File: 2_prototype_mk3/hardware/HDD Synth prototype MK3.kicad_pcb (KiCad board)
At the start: 2 copper layers, 157.5 x 97.8 mm, 47 parts, among them J1 Micro_SD_Card, J3 Bus_ISA_8bit, SW1 SW_Push, U1 Optocoupler_DC_PhotoNPN_AKEC, U5 MAX98357A, U6 74LS573, U7 74LS573, U8 ATF22V10C-10PU

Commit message: MKIII design refinements
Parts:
- removed the   at (140.8, 59.6) (x2)
- added G***: LOGO, HDDSyncMKIII:MKIII logo - 20mm, F.Cu at (85.0, 116.8)
- added G***: LOGO, HDDSyncMKIII:MKIII logo - 30mm, F.Cu at (172.6, 93.9)
- J3: footprint Connector_PCBEdge:BUS_AT -> HDDSyncMKIII:BUS_AT_8bit
- moved H3 52.2 mm to (206.9, 116.8)
- moved C1 51.1 mm to (173.1, 60.6)
- moved FB2 51.1 mm to (173.0, 56.8)
- moved C2 51.1 mm to (173.1, 49.2)
- moved FB1 51.1 mm to (173.0, 52.8)
- moved H6 50.8 mm to (165.0, 53.3)
- moved C6 49.4 mm to (177.7, 47.9), turned to -90 degrees
- moved U5 49.1 mm to (180.1, 55.0)
- moved C5 48.2 mm to (181.5, 47.9), turned to -90 degrees
- moved G*** 37.6 mm to (175.1, 104.1)
- moved   37.5 mm to (133.5, 59.5)
- moved U8 27.4 mm to (159.9, 125.7), turned to 90 degrees
- moved C12 26.5 mm to (157.4, 113.8), turned to 90 degrees
- moved D5 22.3 mm to (162.4, 111.8), turned to -90 degrees
- moved H1 17.8 mm to (179.0, 68.4)
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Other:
- board size 157.5 x 97.8 mm -> 119.4 x 97.8 mm
- board text added: "Make sure the edge cuts for the slot are ok"

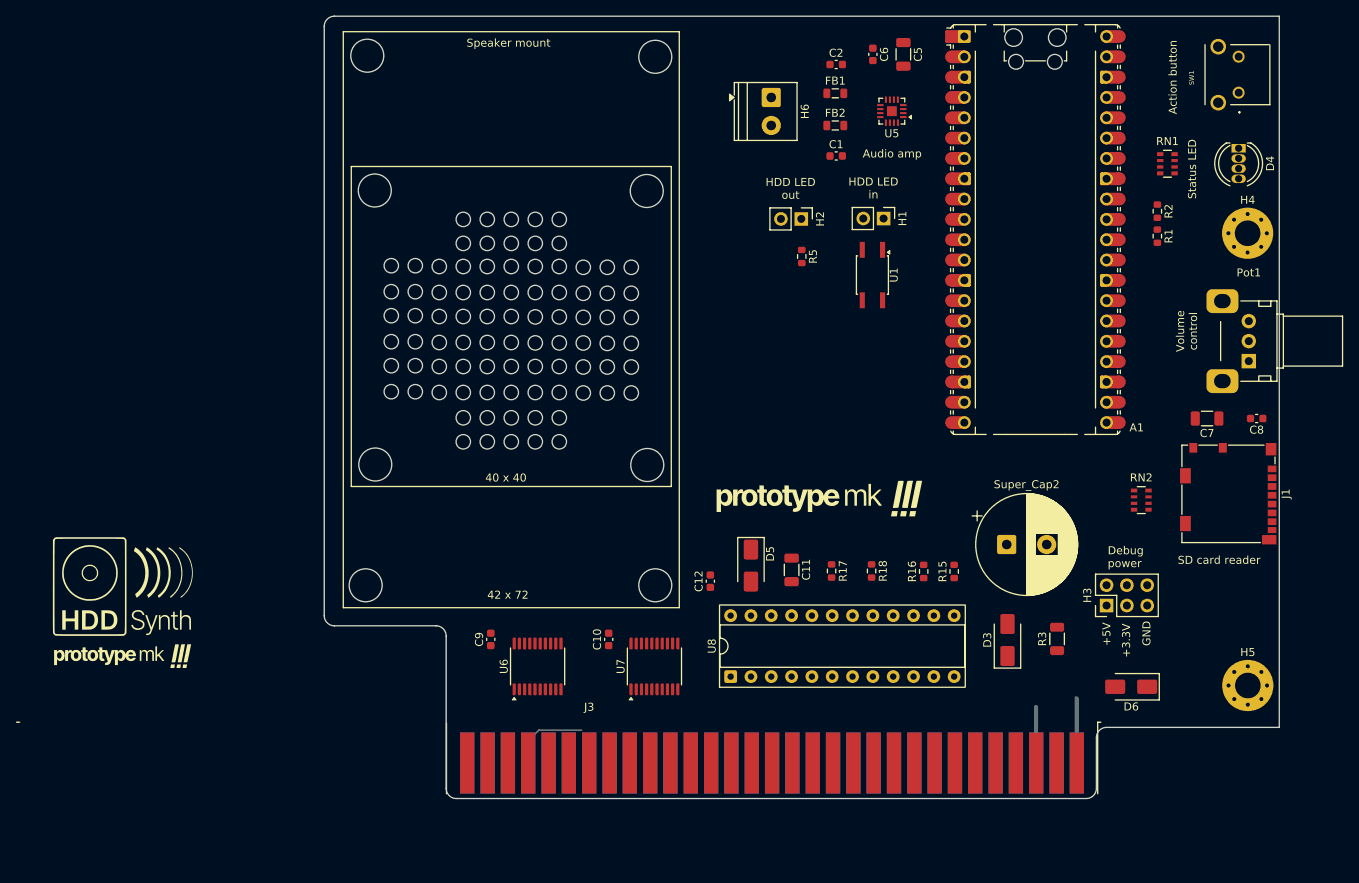
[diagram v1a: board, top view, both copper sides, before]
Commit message: Add net classes for power
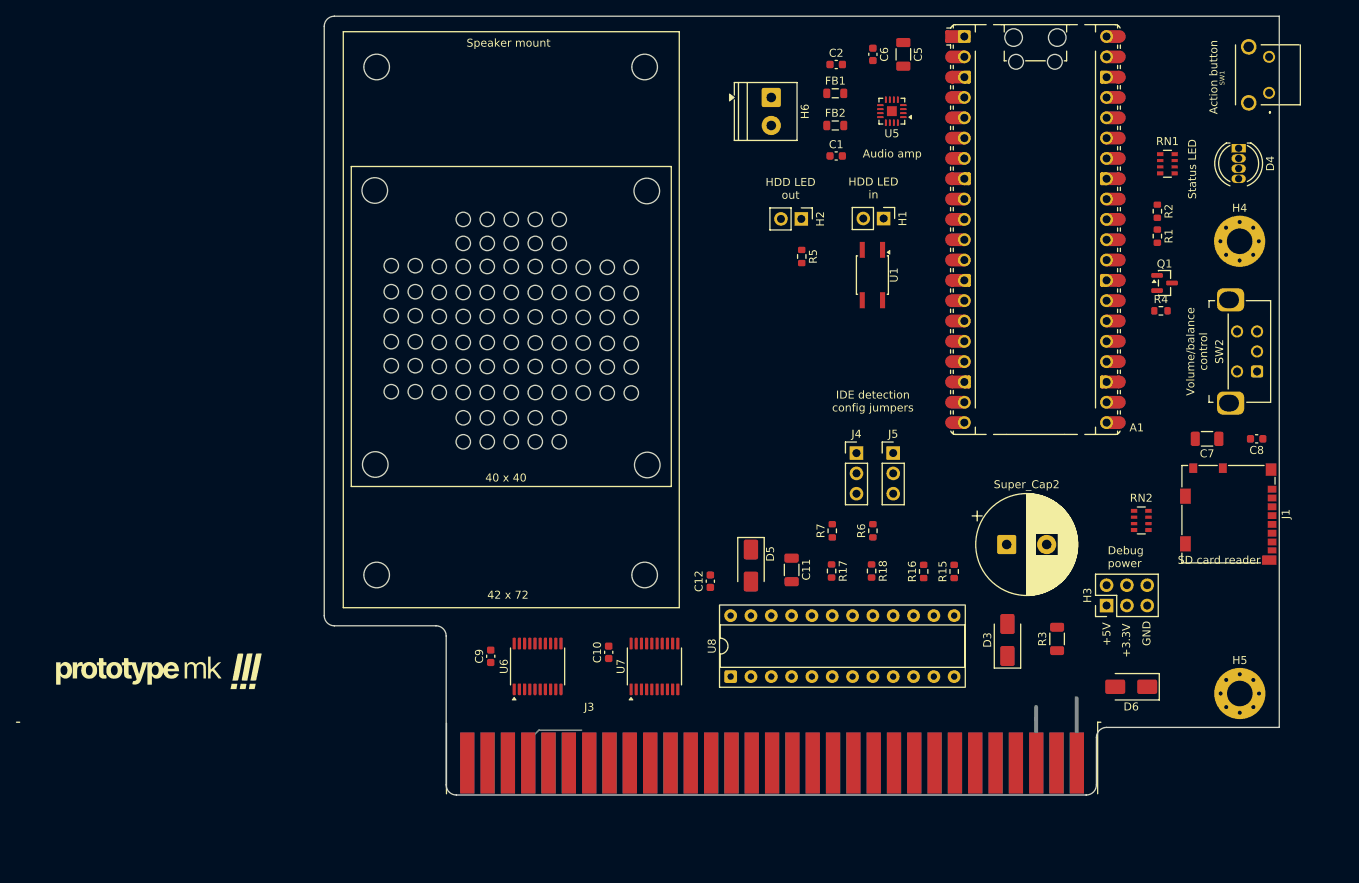
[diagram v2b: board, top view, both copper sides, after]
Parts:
- removed the G*** at (85.0, 116.8)
- removed Pot1: R_Potentiometer, Potentiometer_THT:Potentiometer_Alps_RK09K_Single_Horizontal
- added H10: MountingHole, MountingHole:MountingHole_3.2mm_M3, F.Cu at (149.5, 99.2)
- added H11: MountingHole, MountingHole:MountingHole_3.2mm_M3, F.Cu at (115.7, 49.5)
- added H12: MountingHole, MountingHole:MountingHole_3.2mm_M3, F.Cu at (149.2, 49.5)
- added H13: MountingHole, MountingHole:MountingHole_3.2mm_M3, F.Cu at (115.7, 113.0)
- added H14: MountingHole, MountingHole:MountingHole_3.2mm_M3, F.Cu at (149.2, 113.0)
- added H7: MountingHole, MountingHole:MountingHole_3.2mm_M3, F.Cu at (115.4, 64.9)
- added H8: MountingHole, MountingHole:MountingHole_3.2mm_M3, F.Cu at (149.4, 65.0)
- added H9: MountingHole, MountingHole:MountingHole_3.2mm_M3, F.Cu at (115.5, 99.2)
- added J4: Conn_01x03, Connector_PinHeader_2.54mm:PinHeader_1x03_P2.54mm_Vertical, F.Cu at (175.6, 97.8)
- added J5: Conn_01x03, Connector_PinHeader_2.54mm:PinHeader_1x03_P2.54mm_Vertical, F.Cu at (180.2, 97.8)
- added Q1: 2N3904, Package_TO_SOT_SMD:SOT-23, F.Cu at (214.1, 76.5)
- added R4: 10K, Resistor_SMD:R_0603_1608Metric, F.Cu at (213.7, 80.0)
- added R6: 330R, Resistor_SMD:R_0603_1608Metric, F.Cu at (177.7, 107.5)
- added R7: 3.3K, Resistor_SMD:R_0603_1608Metric, F.Cu at (172.6, 107.5)
- added SW2: RotaryEncoder_Switch, Rotary_Encoder:RotaryEncoder_Bourns_Horizontal_PEC12R-2x17F-Sxxxx, F.Cu at (225.7, 87.5)
- C11: value 10uF -> 2.2uF
- R18: value 330R -> 2.2K
- moved G*** 85.3 mm to (90.0, 115.5)
- moved G*** 36.1 mm to (140.8, 115.5)
- moved SW1 3.81 mm to (227.2, 52.7)
- moved J1 2.54 mm to (222.1, 105.4)
- moved RN2 2.54 mm to (211.2, 106.2)
- moved C7 2.54 mm to (219.5, 96.0)
- moved C8 2.54 mm to (225.7, 96.0)
- moved C9 2.11 mm to (129.9, 123.2)
- moved C10 1.61 mm to (144.7, 122.7)
- moved H4 1.41 mm to (223.5, 71.3)
- moved H5 1.41 mm to (223.5, 127.8)
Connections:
- A1 pad 26: unconnected-(A1-GPIO20-Pad26) -> /ENC_A
- A1 pad 27: unconnected-(A1-GPIO21-Pad27)_1 -> /ENC_B
- A1 pad 29: unconnected-(A1-GPIO22-Pad29)_1 -> /ENC_SWITCH
- A1 pad 30: unconnected-(A1-RUN-Pad30)_1 -> Net-(A1-RUN)
- A1 pad 32: /VOL_POT -> unconnected-(A1-GPIO27_ADC1-Pad32)
- D5 pad 2: /ISA IDE activity detection/IDE_ACTIVITY_RAW -> Net-(D5-A)
- J1 pad 2: /SD card reader/SD_CS -> /SD_CS
- J3 pad 2: unconnected-(J3-RESET-Pad2) -> /ISA IDE activity detection/RESET
- RN2 pad 1: /SD card reader/SD_CS -> /SD_CS
- U8 pad 21: unconnected-(U8-IO7-Pad21) -> Net-(J4-Pin_2)
- U8 pad 22: /ISA IDE activity detection/IDE_ACTIVITY_RAW -> Net-(J5-Pin_2)
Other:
- board size 119.4 x 97.8 mm -> 119.4 x 97.4 mm
- board text added: "IDE detection config jumpers"
- board text added: "Special thanks to: - Cecilia MacLoughlin - Ian (polpo) Scott - Ian (PSYCHROME) Ball - Mark Angus - Neil Thomas (Retro Collective) - vswitchzero - Wouter Groeneveld - VOGONS and SWAG"
- board text added: "Volume/balance control"
- board text added: "www.strifestreams.com/hddsynth"
- board text removed: "Volume control"

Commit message: MKIII PCB components connected and passing DRC
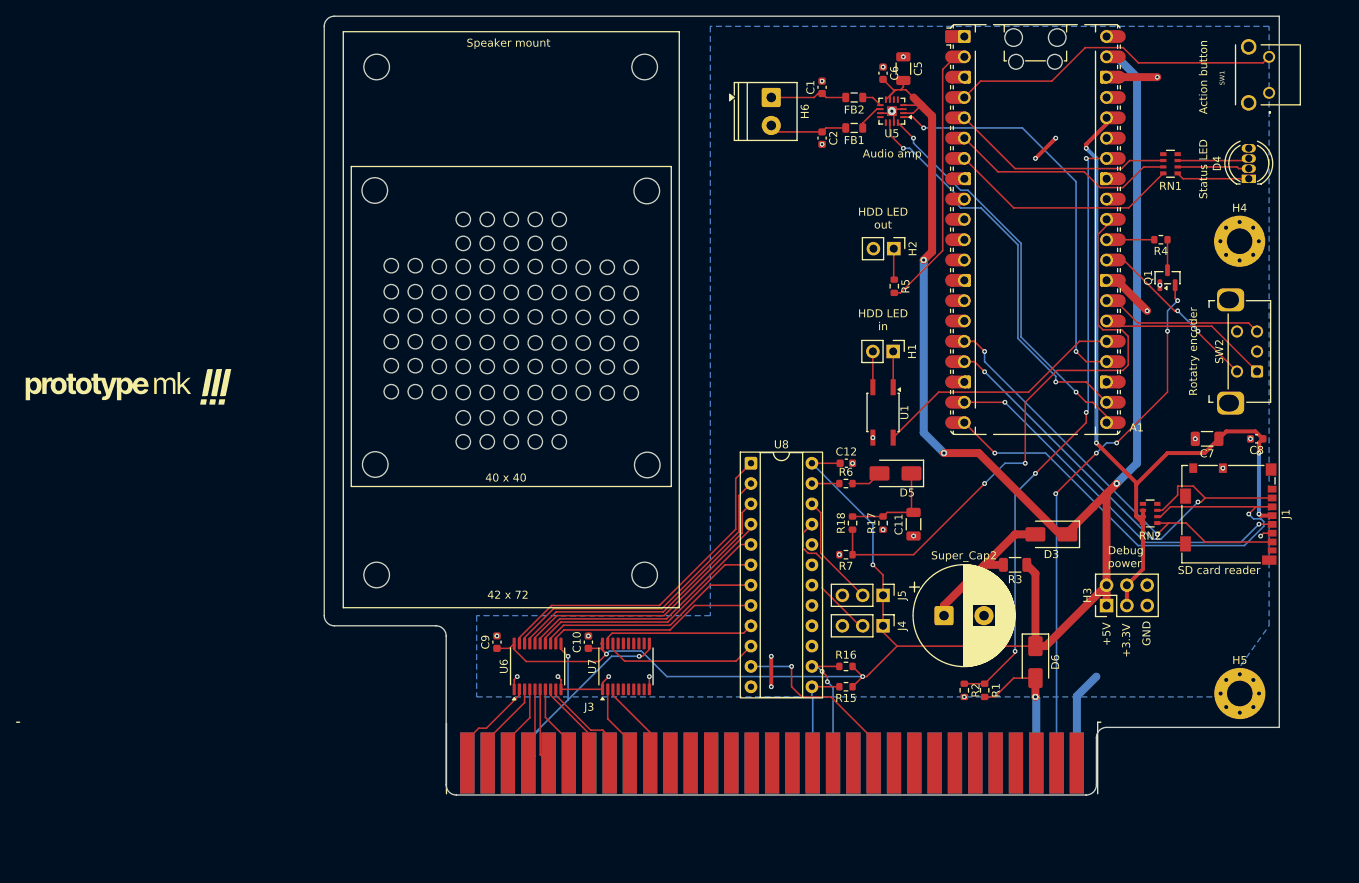
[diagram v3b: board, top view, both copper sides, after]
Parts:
- moved R2 64.6 mm to (189.1, 127.4)
- moved R1 60.7 mm to (191.7, 127.4)
- moved G*** 35.8 mm to (86.2, 80.0)
- moved U8 26.8 mm to (162.4, 99.0), turned to 0 degrees
- moved C12 22.5 mm to (174.4, 99.0), turned to 0 degrees
- moved J4 21.8 mm to (178.9, 119.3), turned to -90 degrees
- moved D5 21.4 mm to (180.5, 100.3), turned to 180 degrees
- moved R15 19.8 mm to (174.3, 127.0), turned to 180 degrees
- moved J5 17.8 mm to (178.9, 115.5), turned to -90 degrees
- moved U1 17.2 mm to (178.9, 92.7)
- moved H1 16.7 mm to (180.2, 85.0)
- moved C11 16.3 mm to (182.8, 106.6), turned to 90 degrees
- moved R16 15.3 mm to (174.3, 124.4), turned to 0 degrees
- moved D3 14.3 mm to (200.0, 107.9), turned to 180 degrees
- moved D6 12.4 mm to (198.0, 123.9), turned to -90 degrees
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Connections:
- A1 pad 39: /Power management/VSYS_5V_INPUT -> POWER_5V_SUP
- C1 pad 1: Net-(H6-Pin_2) -> Net-(H6-Pin_1)
- C10 pad 1: +5V -> POWER_5V_SUP
- C12 pad 1: +5V -> POWER_5V_SUP
- C2 pad 1: Net-(H6-Pin_1) -> Net-(H6-Pin_2)
- C5 pad 2: +5V -> POWER_5V_SUP
- C6 pad 2: +5V -> POWER_5V_SUP
- C9 pad 1: +5V -> POWER_5V_SUP
- D3 pad 1: /Power management/VSYS_5V_INPUT -> POWER_5V_SUP
- D6 pad 1: /Power management/VSYS_5V_INPUT -> POWER_5V_SUP
- FB1 pad 2: Net-(H6-Pin_1) -> Net-(H6-Pin_2)
- FB2 pad 2: Net-(H6-Pin_2) -> Net-(H6-Pin_1)
- H3 pad 1: /Power management/VSYS_5V_INPUT -> POWER_5V_SUP
- H3 pad 2: /Power management/VSYS_5V_INPUT -> POWER_5V_SUP
- J4 pad 1: +5V -> POWER_5V_SUP
- J5 pad 1: +5V -> POWER_5V_SUP
- R15 pad 1: +5V -> POWER_5V_SUP
- R16 pad 2: +5V -> POWER_5V_SUP
- R3 pad 1: /Power management/VSYS_5V_INPUT -> POWER_5V_SUP
- RN2 pad 1: /SD_CS -> /SD_SO
- RN2 pad 3: /SD_SO -> /SD_CS
- U5 pad 2: +5V -> POWER_5V_SUP
- U5 pad 4: +5V -> POWER_5V_SUP
- U5 pad 7: +5V -> POWER_5V_SUP
- U5 pad 8: +5V -> POWER_5V_SUP
- U6 pad 20: +5V -> POWER_5V_SUP
- U7 pad 20: +5V -> POWER_5V_SUP
- U8 pad 24: +5V -> POWER_5V_SUP
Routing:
- net POWER_5V_SUP: track 0.00 -> 295.1 mm, vias 0 -> 6
- net +3.3V: track 0.00 -> 98.0 mm, vias 0 -> 4
- net /ISA_VCC_DETECT: track 0.00 -> 76.2 mm, vias 0 -> 4
- net /IDE_ACTIVITY: track 0.00 -> 74.5 mm, vias 0 -> 2
- net /ISA IDE activity detection/RESET: track 0.00 -> 67.0 mm, vias 0 -> 5
- net /SD_SI: track 0.00 -> 63.8 mm, vias 0 -> 2
- net /SD_CS: track 0.00 -> 58.3 mm, vias 0 -> 2
- net /SD_SO: track 0.00 -> 52.2 mm, vias 0 -> 2
- net /AMP_DIN: track 0.00 -> 50.5 mm, vias 0 -> 2
- net /AMP_LRC: track 0.00 -> 50.4 mm, vias 0 -> 2
- net /AMP_BCLK: track 0.00 -> 49.6 mm, vias 0 -> 2
- net /SD_CLK: track 0.00 -> 46.7 mm, vias 0 -> 2
- net /ISA IDE activity detection/ISA_AL0: track 0.00 -> 42.4 mm
- net GND: track 8.32 -> 50.6 mm, vias 0 -> 28
- net /ACTION_BUTTON: track 0.00 -> 41.8 mm
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- added copper zone on B.Cu, net GND
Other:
- board text added: "Rotatry encoder"
- board text removed: "IDE detection config jumpers"
- board text removed: "Volume/balance control"

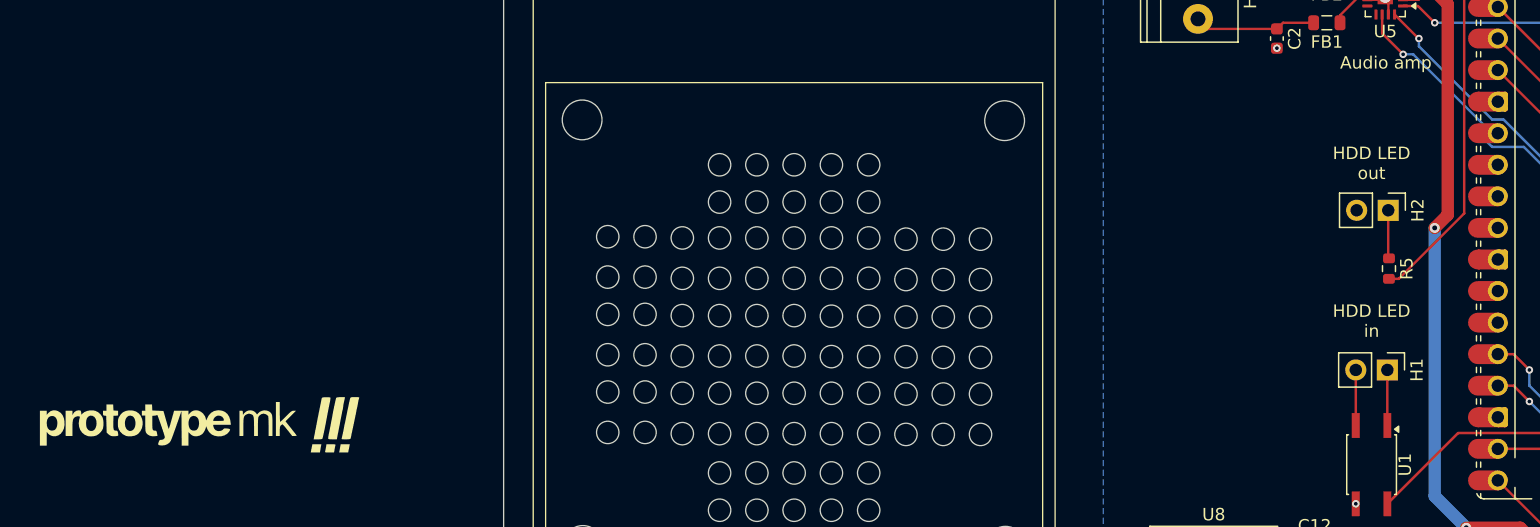
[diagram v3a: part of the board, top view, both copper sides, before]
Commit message: Finalise silk screen and tidy up files
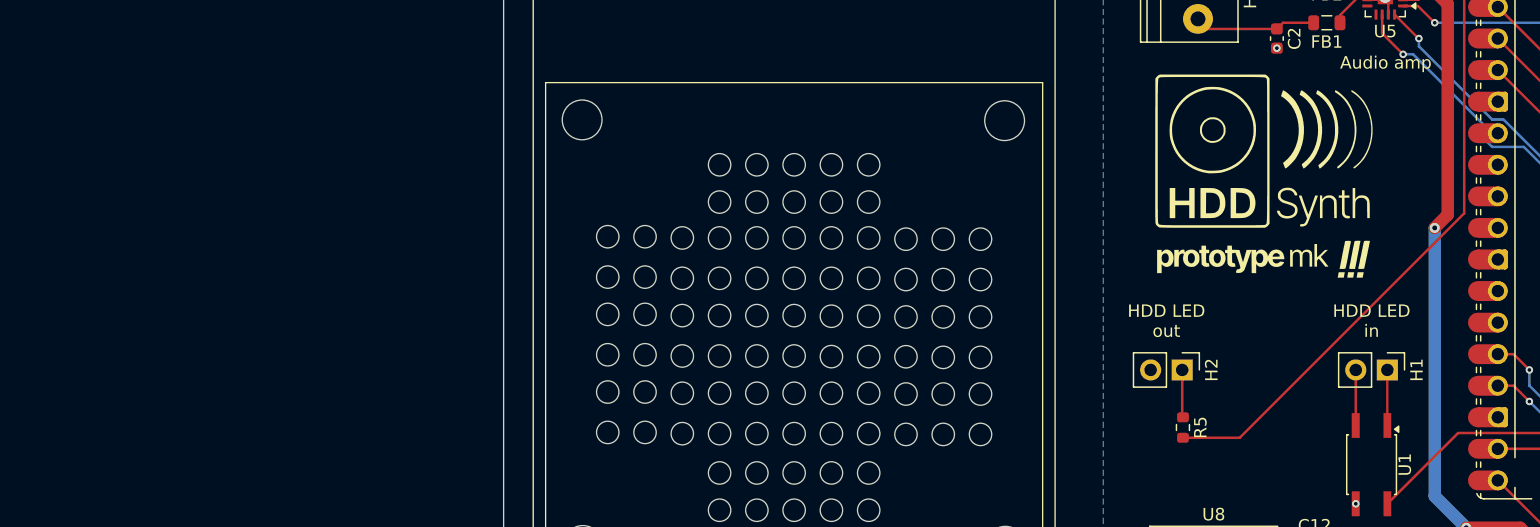
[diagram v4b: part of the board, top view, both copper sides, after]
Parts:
- removed the G*** at (86.2, 80.0)
- added G***: LOGO, HDDSyncMKIII:MKIII logo - 20mm, F.Cu at (171.3, 69.8)
- SW2: value RotaryEncoder_Switch -> PEC12R-2120F-S0012
- moved H2 21.0 mm to (163.7, 85.0)
- moved R5 20.9 mm to (163.8, 89.7)
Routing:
- net /HDD_LED_OUT: track 34.3 -> 56.1 mm
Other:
- board text removed: "Make sure the edge cuts for the slot are ok"
